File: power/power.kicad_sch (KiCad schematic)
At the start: 178 parts, among them J1 USB-C Power + USB2.0, J2 USB, J3 BATTERY OUT, J4 BACKUP, J5 I2C, Q1 SI7617DN-T1-GE3, Q2 CSD18534Q5A, Q3 CSD18534Q5A, Q4 CSD18534Q5A, Q5 CSD18534Q5A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

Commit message: embedded controller work
Update power.kicad_sch
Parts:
- removed C6: 1uF, Capacitor_SMD:C_0603_1608Metric, symbol Device:C_Small
- removed R57: 1k, Resistor_SMD:R_0603_1608Metric, symbol Device:R_Small
- removed U8: CP2102N-Axx-xQFN28, Package_DFN_QFN:QFN-28-1EP_5x5mm_P0.5mm_EP3.35x3.35mm, symbol Interface_USB:CP2102N-Axx-xQFN28
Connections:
- net SCL: now also U2.4 (SCL); no longer U2.5 (SDA)
- net SDA: now also U2.5 (SDA); no longer U2.4 (SCL)
- net at U2.1 (SENSE+): now also R9.3; no longer R9.2
- net at U2.8 (SENSE-): now also R9.2; no longer R9.3
- no-connect marks 42 -> 24
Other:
- note added: "@TODO: decrease shunt"
- note added: "@TODO: external 3.3 choice"
- note added: "@TODO: flip"
- note added: "better buck"
- moved on the sheet: C1, C2, C3, C4, C5, D14, J1, J2, L1, R1, R11, R12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

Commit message: power 3d file
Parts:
- added C6: 1uF, Capacitor_SMD:C_0603_1608Metric, symbol Device:C_Small
- added R57: 1k, Resistor_SMD:R_0603_1608Metric, symbol Device:R_Small
- added U8: CP2102N-Axx-xQFN28, Package_DFN_QFN:QFN-28-1EP_5x5mm_P0.5mm_EP3.35x3.35mm, symbol Interface_USB:CP2102N-Axx-xQFN28
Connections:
- net +3.3V: now also C6.1, R57.2, U8.6 (VDD), U8.7 (VREGIN)
- net GND: now also C6.2, U8.29 (GND), U8.3 (GND)
- net RXD0: now also U8.26 (TXD)
- net TXD0: now also U8.25 (RXD)
- net USB_D+: now also U8.5 (D-)
- net USB_D-: now also U8.4 (D+)
- net USB_VBUS: now also U8.8 (VBUS)
- new net: R57.1, U8.9 (~{RST})
- no-connect marks 24 -> 42
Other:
- note added: "@TODO: use USB-CDC"
- note removed: "@TODO: decrease shunt"
- moved on the sheet: C1, C2, C3, C4, C5, D14, J1, J2, L1, R1, R11, R12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

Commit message: powertrain v2
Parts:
- removed U7: TPS560200, Package_TO_SOT_SMD:SOT-23-5, symbol Regulator_Switching:TPS560200
- removed U8: CP2102N-Axx-xQFN28, Package_DFN_QFN:QFN-28-1EP_5x5mm_P0.5mm_EP3.35x3.35mm, symbol Interface_USB:CP2102N-Axx-xQFN28
- added C58: 100nF, Capacitor_SMD:C_0402_1005Metric, symbol Device:C_Small
- added R72: 12k, Resistor_SMD:R_0402_1005Metric, symbol Device:R_Small
- added U7: TPS564257DRLR, TPS564257:SOT50P160X60-6N, symbol TPS564257:TPS564257DRLR
- C4: value 10uF -> 100nF; footprint Capacitor_SMD:C_0603_1608Metric -> Capacitor_SMD:C_0402_1005Metric; LCSC C913517 -> C307331
- C5: value 0.1uF -> 22uF; LCSC C14663 -> C162690
- C6: value 1uF -> 22uF; LCSC C15849 -> C162690
- D14: LCSC C72038 -> (none)
- L1: value FTC252012S100MBCA -> SLO0530H3R3MTT; footprint Inductor_SMD:L_1008_2520Metric -> Inductor_SMD:L_Chilisin_BMRA00050530; LCSC C5832376 -> C408446
- R11: value 7.5k -> 47k; footprint Resistor_SMD:R_0603_1608Metric -> Resistor_SMD:R_0402_1005Metric; LCSC C23234 -> C25744
- R12: value 24k -> 10k; footprint Resistor_SMD:R_0603_1608Metric -> Resistor_SMD:R_0402_1005Metric; LCSC C23352 -> C25744
- R13: value 56k -> 49.9k; footprint Resistor_SMD:R_0603_1608Metric -> Resistor_SMD:R_0402_1005Metric; LCSC C23206 -> C25897
- R14: value 10k -> 510k; footprint Resistor_SMD:R_0603_1608Metric -> Resistor_SMD:R_0402_1005Metric; LCSC C25804 -> C11616
- R57: value 1k -> 10k; footprint Resistor_SMD:R_0603_1608Metric -> Resistor_SMD:R_0402_1005Metric
- R71: value 1k -> 47k; footprint Resistor_SMD:R_0603_1608Metric -> Resistor_SMD:R_0402_1005Metric; LCSC C25744 -> C25897
- R9: value 50mΩ SHUNT LR122WF500MT4E -> 10mΩ SHUNT FMF25FPJR010-LH; LCSC C2941069 -> C105366
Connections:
- net +3.3V: now also C5.1, R11.2, R13.2, R14.2, C58.1; no longer C2.1, C3.1, R57.2, R71.1
- net C4: now also R9.4; no longer R9.1
- net GND: now also R57.1, C58.2, R72.1, U7.3 (GND); no longer R11.1, R14.1
- net USB_D+: now also U5.24 (IO20)
- net USB_D-: now also U5.23 (IO19)
- net VDD: now also C2.1, C3.1, R71.2, R9.1, U7.1 (VIN); no longer C5.1, R13.2, R9.4
- net at R13.1: now also R14.1, R57.2, U7.6 (FB); no longer R14.2
- net 3V3_SW: now reaches L1.1
- net 3V3_SW: now also U7.2 (SW)
- net at U2.1 (SENSE+): now also R9.2; no longer R9.3
- net at U2.8 (SENSE-): now also R9.3; no longer R9.2
- net at D14.2 (A): now also R11.1; no longer R71.2
- net FB: no longer names the net of R12.1
- net FB: now also U7.4 (PG); no longer R11.2
- new net: R71.1, R72.2, U7.5 (EN)
- no-connect marks 42 -> 22
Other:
- note added: "5A max"
- note added: "USB-CDC based"
- note removed: "@TODO check shunts"
- note removed: "@TODO: external 3.3 choice"
- note removed: "@TODO: flip"
- note removed: "@TODO: use USB-CDC"
- note removed: "better buck"
- moved on the sheet: H1, H2, H3, J2, J5, R50, R51, SW1, SW2

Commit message: powertrain v0.2 tapeout
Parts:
- C10, C26: LCSC C307331 -> C14663
- C11, C12, C13, C14, C15, C16, C17, C23, C27, C46, C48: LCSC C913517 -> C15849
- C18, C19, C20, C21, C22, C55: LCSC C913517 -> C14663
- C2, C24, C25, C28, C29, C3, C30, C31, C32, C33, C40, C41, C42, C43, C44, C45, C56, C8, C9: LCSC C913517 -> C96446
- C34, C35: LCSC C913517 -> C21117
- C36: LCSC C913517 -> C1623
- C37: LCSC C913517 -> C57112
- C38, C39: LCSC C913517 -> C1622
- C47: LCSC C913517 -> C23630
- C49: LCSC C913517 -> C1630
- C5, C6: LCSC C162690 -> C59461
- C50: LCSC C913517 -> C1644
- C51: LCSC C913517 -> C1663
- C52: LCSC C913517 -> C1599
- C53, C54: LCSC C913517 -> C14858
- D14: LCSC (none) -> C72038
- J3: LCSC C564042 -> C564032
- R11: LCSC C25744 -> C25792
- R33: LCSC C25744 -> C22939
- R35, R36: LCSC C25744 -> C25197
- R38, R39, R44: LCSC C25744 -> C22859
- R40: LCSC C25744 -> C22795
- R41: LCSC C25744 -> C23178
- R42: LCSC C25744 -> C23150
- R43: LCSC C25744 -> C22961
- R45: LCSC C25744 -> C22976
- R46: LCSC C25744 -> C23024
- R47, R48, R49, R50, R51, R52, R58, R59, R60, R61, R62, R63: LCSC C25744 -> C25804
- R53: LCSC C25744 -> C12447
- R54: LCSC C25744 -> C8218
- R55: LCSC C25744 -> C25805
- R56: LCSC C25744 -> C22967
- R64, R65: LCSC C25744 -> C21189
- R66, R67, R68, R69, R70: LCSC C25744 -> C21190
- R71: LCSC C25897 -> C25792
- R72: LCSC C25897 -> C25752
- U5: LCSC C3013941 -> C2980299

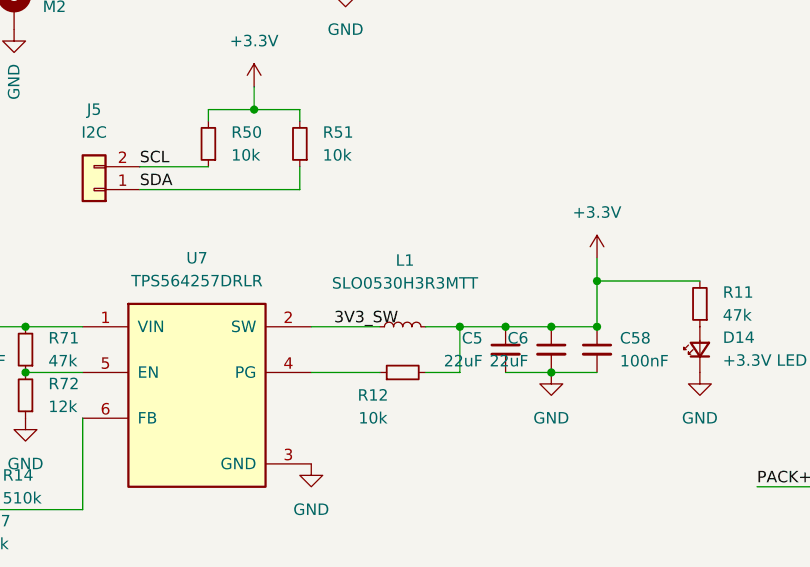
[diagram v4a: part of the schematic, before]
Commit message: fixed pt v0.2 inductor
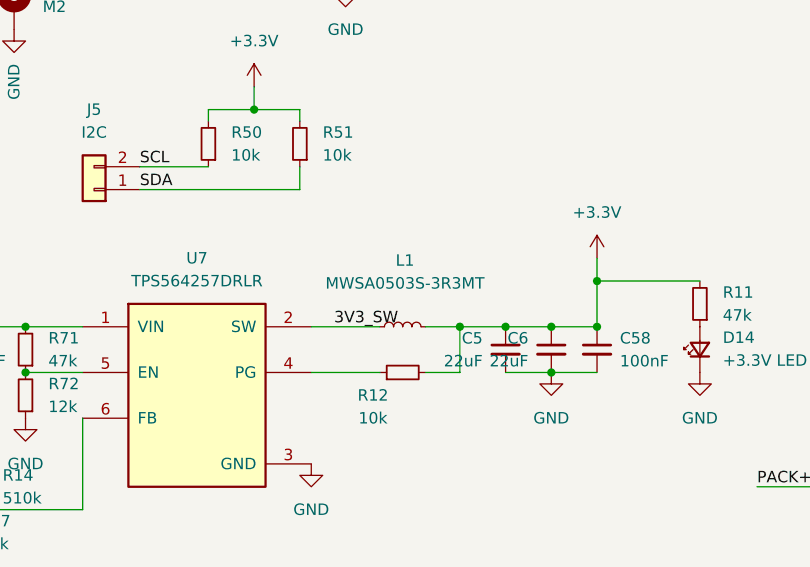
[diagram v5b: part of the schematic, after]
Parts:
- L1: value SLO0530H3R3MTT -> MWSA0503S-3R3MT; footprint Inductor_SMD:L_Chilisin_BMRA00050530 -> Inductor_SMD:L_Sunlord_MWSA0503S; LCSC C408446 -> C408409
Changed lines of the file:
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@@
 			)
 		)
-		(property "Value" "SLO0530H3R3MTT"
+		(property "Value" "MWSA0503S-3R3MT"
 			(at 45.974 141.224 90)
 			(effects
@@
 			)
 		)
-		(property "Footprint" "Inductor_SMD:L_Chilisin_BMRA00050530"
+		(property "Footprint" "Inductor_SMD:L_Sunlord_MWSA0503S"
 			(at 45.72 146.05 0)
 			(effects
@@
 			)
 		)
-		(property "LCSC" "C408446"
+		(property "LCSC" "C408409"
 			(at 45.72 140.97 0)
 			(effects
